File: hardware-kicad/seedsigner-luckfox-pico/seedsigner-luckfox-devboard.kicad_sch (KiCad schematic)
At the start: 37 parts, among them J1 Conn_01x10, J2 Conn_01x05, U1 LuckFox_Pico, U2 RASPBERRY_PI_3_MODEL_B+

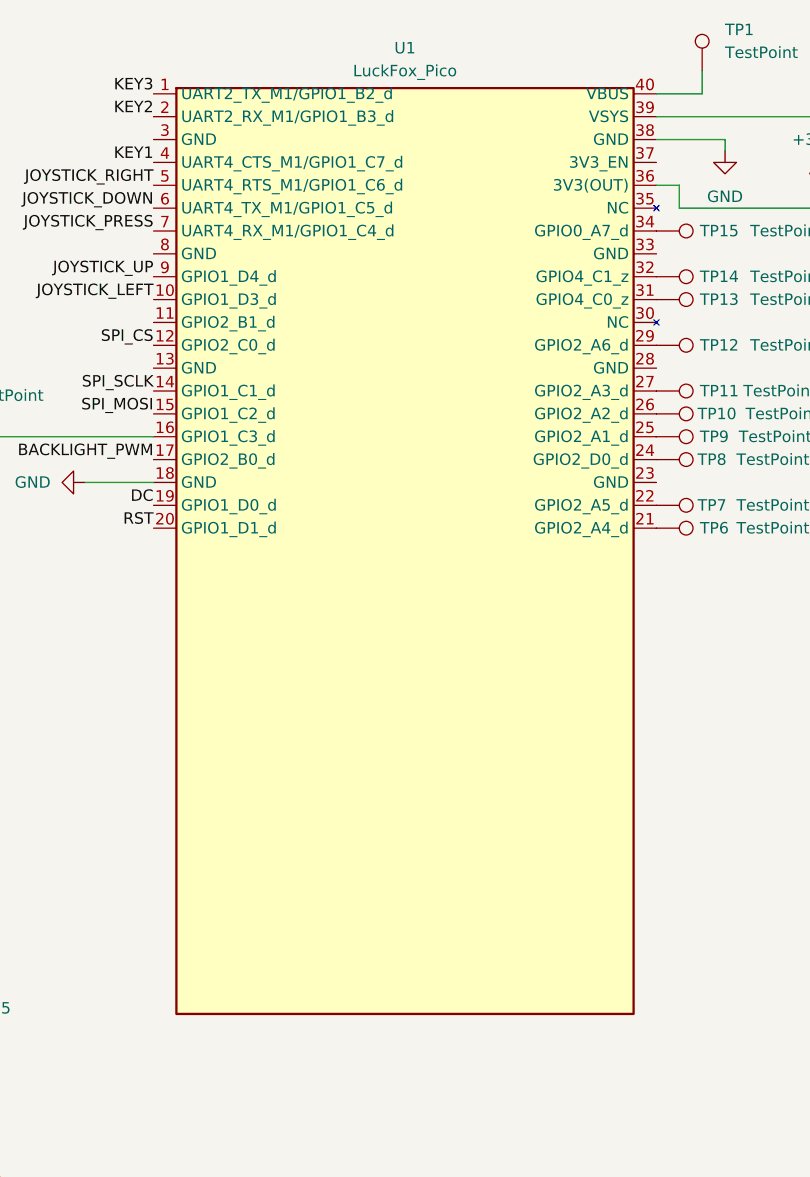
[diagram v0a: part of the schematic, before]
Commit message: update libraries and make schematic and pcb only use parts from library
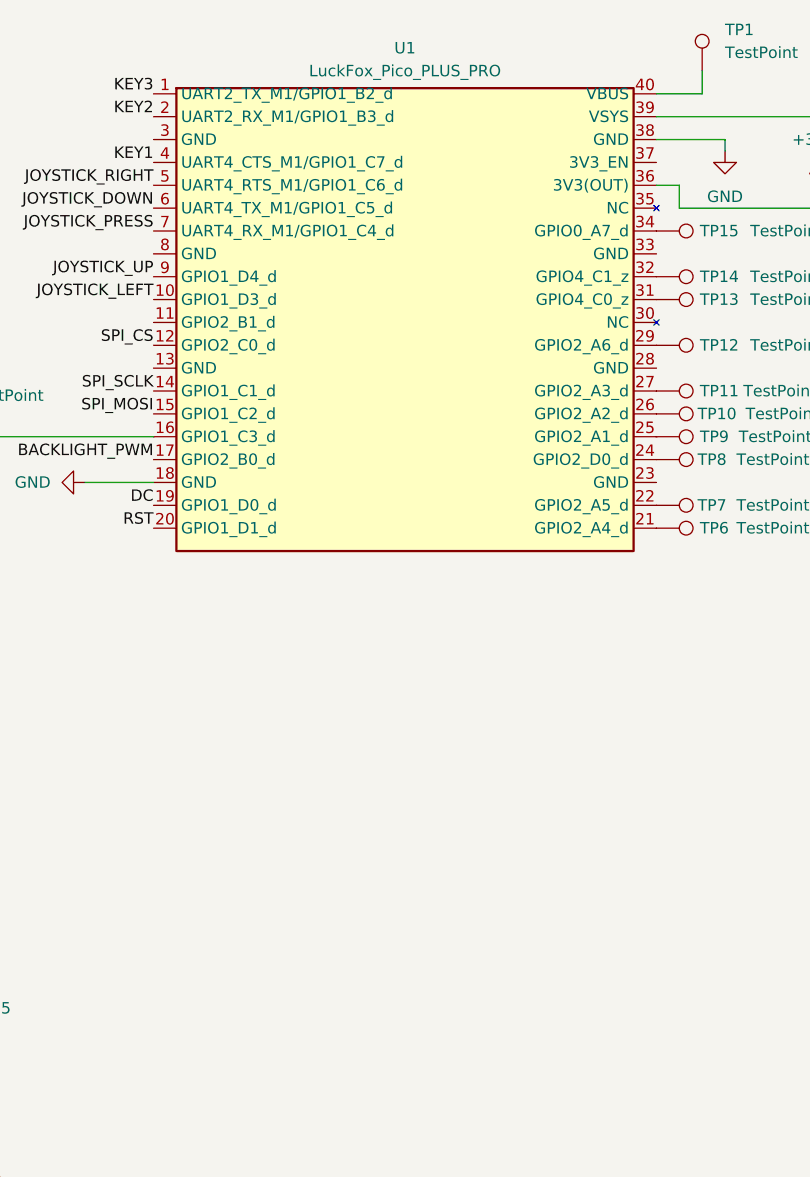
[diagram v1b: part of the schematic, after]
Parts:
- removed U1: LuckFox_Pico, SeedSigner:LUCKFOX_PICO_PRO_MAX_PTH, symbol luckfox:LuckFox_Pico
- added U1: LuckFox_Pico_PLUS_PRO, seedsigner-luckfox:LUCKFOX_PICO_PRO_MAX_PTH, symbol Luckfox:LuckFox_Pico_PLUS_PRO
- ART1: footprint SeedSigner:LightningSpore_Logo -> seedsigner-luckfox:LightningSpore_Logo
- C1: footprint Capacitor_THT:CP_Radial_D5.0mm_P2.50mm -> seedsigner-luckfox:CP_Radial_D5.0mm_P2.50mm
- H1, H2, H3, H4: footprint SeedSigner:MOUNT_HOLE_3MM -> seedsigner-luckfox:MOUNT_HOLE_3MM
- J1: footprint Connector_PinHeader_2.54mm:PinHeader_1x10_P2.54mm_Horizontal -> seedsigner-luckfox:PinHeader_1x10_P2.54mm_Horizontal
- J2: footprint Connector_PinHeader_2.54mm:PinHeader_1x05_P2.54mm_Horizontal -> seedsigner-luckfox:PinHeader_1x05_P2.54mm_Horizontal
- JP1: footprint Jumper:SolderJumper-2_P1.3mm_Bridged_Pad1.0x1.5mm -> seedsigner-luckfox:SolderJumper-2_P1.3mm_Bridged_Pad1.0x1.5mm
- JP2: footprint Jumper:SolderJumper-2_P1.3mm_Open_Pad1.0x1.5mm -> seedsigner-luckfox:SolderJumper-2_P1.3mm_Open_Pad1.0x1.5mm
- LOGO1: footprint SeedSigner:seedsigner-logo-small -> seedsigner-luckfox:seedsigner-logo-small
- LOGO2: footprint SeedSigner:corn-logo -> seedsigner-luckfox:corn-logo
- R1, R2, R3, R4, R5, R6, R7, R8: footprint Resistor_SMD:R_2512_6332Metric -> seedsigner-luckfox:R_2512_6332Metric
- TP1, TP10, TP11, TP12, TP13, TP14, TP15, TP2, TP3, TP4, TP5, TP6, TP7, TP8, TP9: footprint TestPoint:TestPoint_Pad_1.5x1.5mm -> seedsigner-luckfox:TestPoint_Pad_1.5x1.5mm
- U2: footprint SeedSigner:WAVESHARE_LCD_BUTTON -> seedsigner-luckfox:WAVESHARE_LCD_BUTTON
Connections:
- net +3.3V: now also U1.36 (3V3(OUT))
- net BACKLIGHT_PWM: now also U1.17 (GPIO2_B0_d)
- net DC: now also U1.19 (GPIO1_D0_d)
- net GND: now also U1.18 (GND), U1.38 (GND)
- net JOYSTICK_DOWN: now also U1.6 (UART4_TX_M1/GPIO1_C5_d)
- net JOYSTICK_LEFT: now also U1.10 (GPIO1_D3_d)
- net JOYSTICK_PRESS: now also U1.7 (UART4_RX_M1/GPIO1_C4_d)
- net JOYSTICK_RIGHT: now also U1.5 (UART4_RTS_M1/GPIO1_C6_d)
- net JOYSTICK_UP: now also U1.9 (GPIO1_D4_d)
- net KEY1: now also U1.4 (UART4_CTS_M1/GPIO1_C7_d)
- net KEY2: now also U1.2 (UART2_RX_M1/GPIO1_B3_d)
- net KEY3: now also U1.1 (UART2_TX_M1/GPIO1_B2_d)
- net RST: now also U1.20 (GPIO1_D1_d)
- net SPI_CS: now also U1.12 (GPIO2_C0_d)
- net SPI_MOSI: now also U1.15 (GPIO1_C2_d)
- net SPI_SCLK: now also U1.14 (GPIO1_C1_d)
- net at TP2.1: now also U1.39 (VSYS)
- net at TP13.1: now also U1.31 (GPIO4_C0_z)
- net at TP1.1: now also U1.40 (VBUS)
- net at TP15.1: now also U1.34 (GPIO0_A7_d)
- net at TP8.1: now also U1.24 (GPIO2_D0_d)
- net at TP7.1: now also U1.22 (GPIO2_A5_d)
- net at TP9.1: now also U1.25 (GPIO2_A1_d)
- net at TP10.1: now also U1.26 (GPIO2_A2_d)
- net at TP14.1: now also U1.32 (GPIO4_C1_z)
- net at TP12.1: now also U1.29 (GPIO2_A6_d)
- net at TP6.1: now also U1.21 (GPIO2_A4_d)
- net at TP5.1: now also U1.16 (GPIO1_C3_d)
- net at TP11.1: now also U1.27 (GPIO2_A3_d)
